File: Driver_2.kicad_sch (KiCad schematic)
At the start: 26 parts

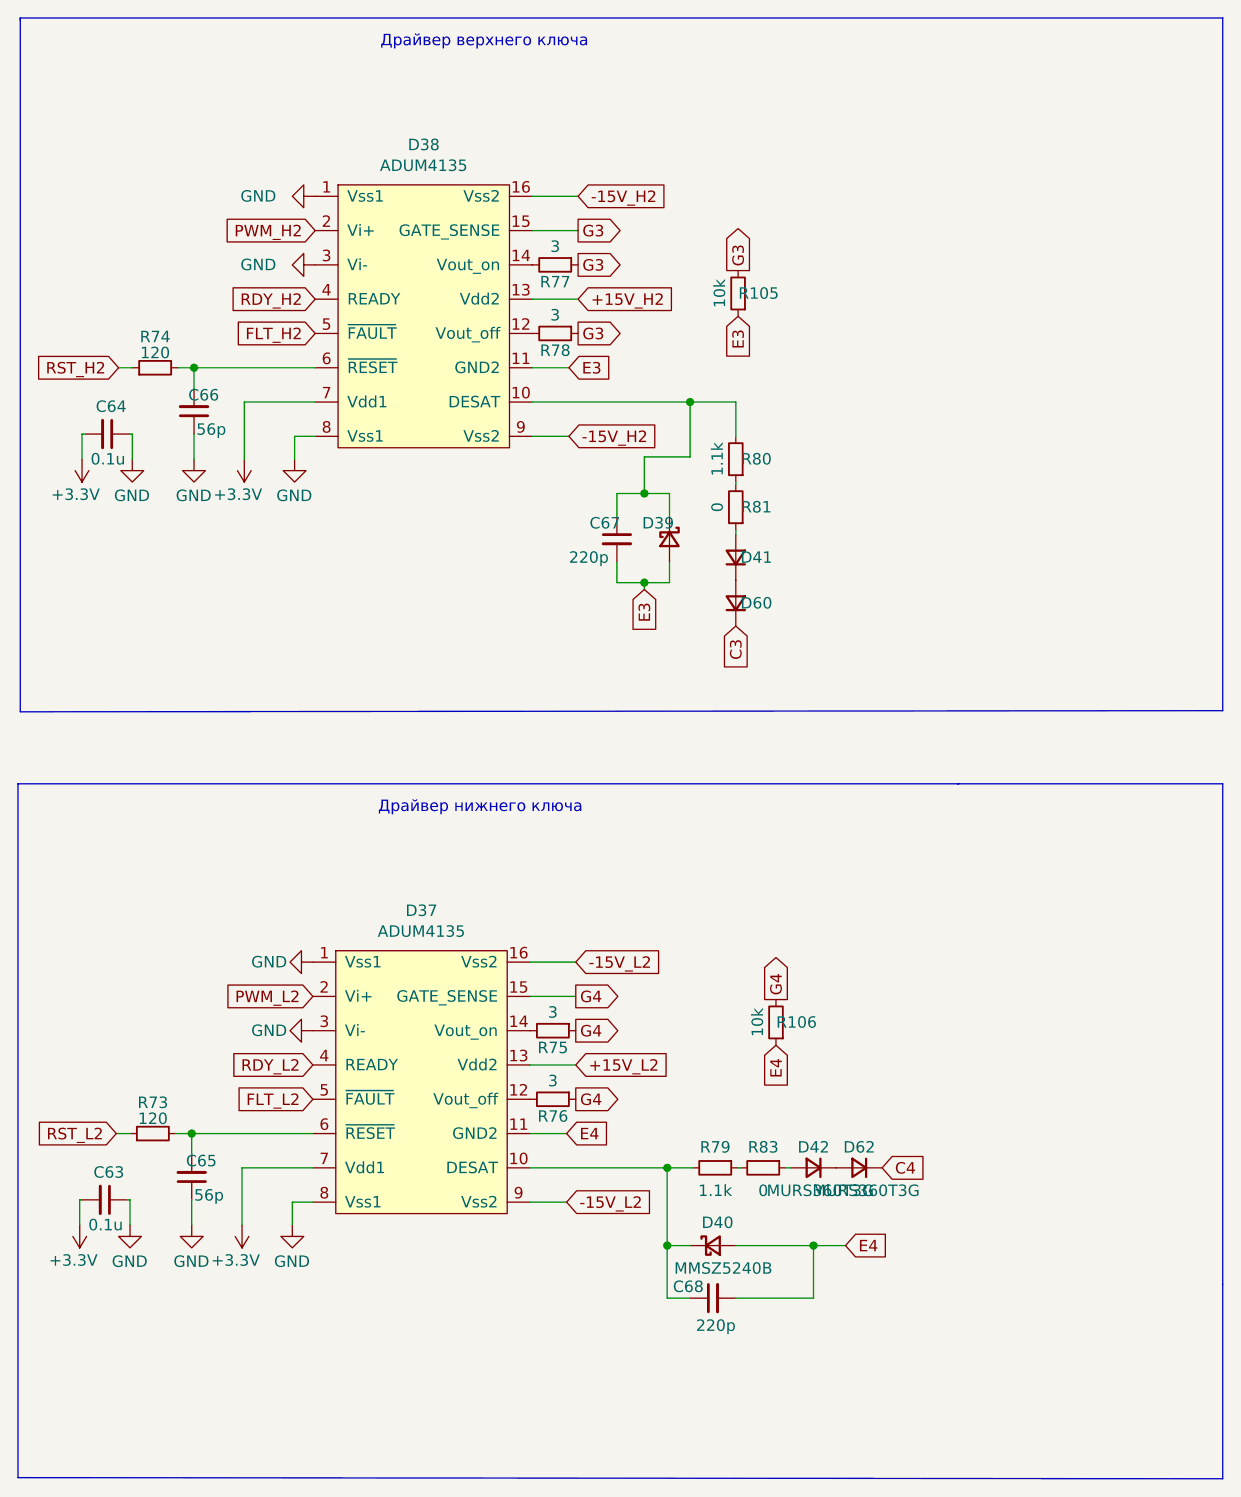
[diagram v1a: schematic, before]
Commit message: Поменял драйвера на китайские
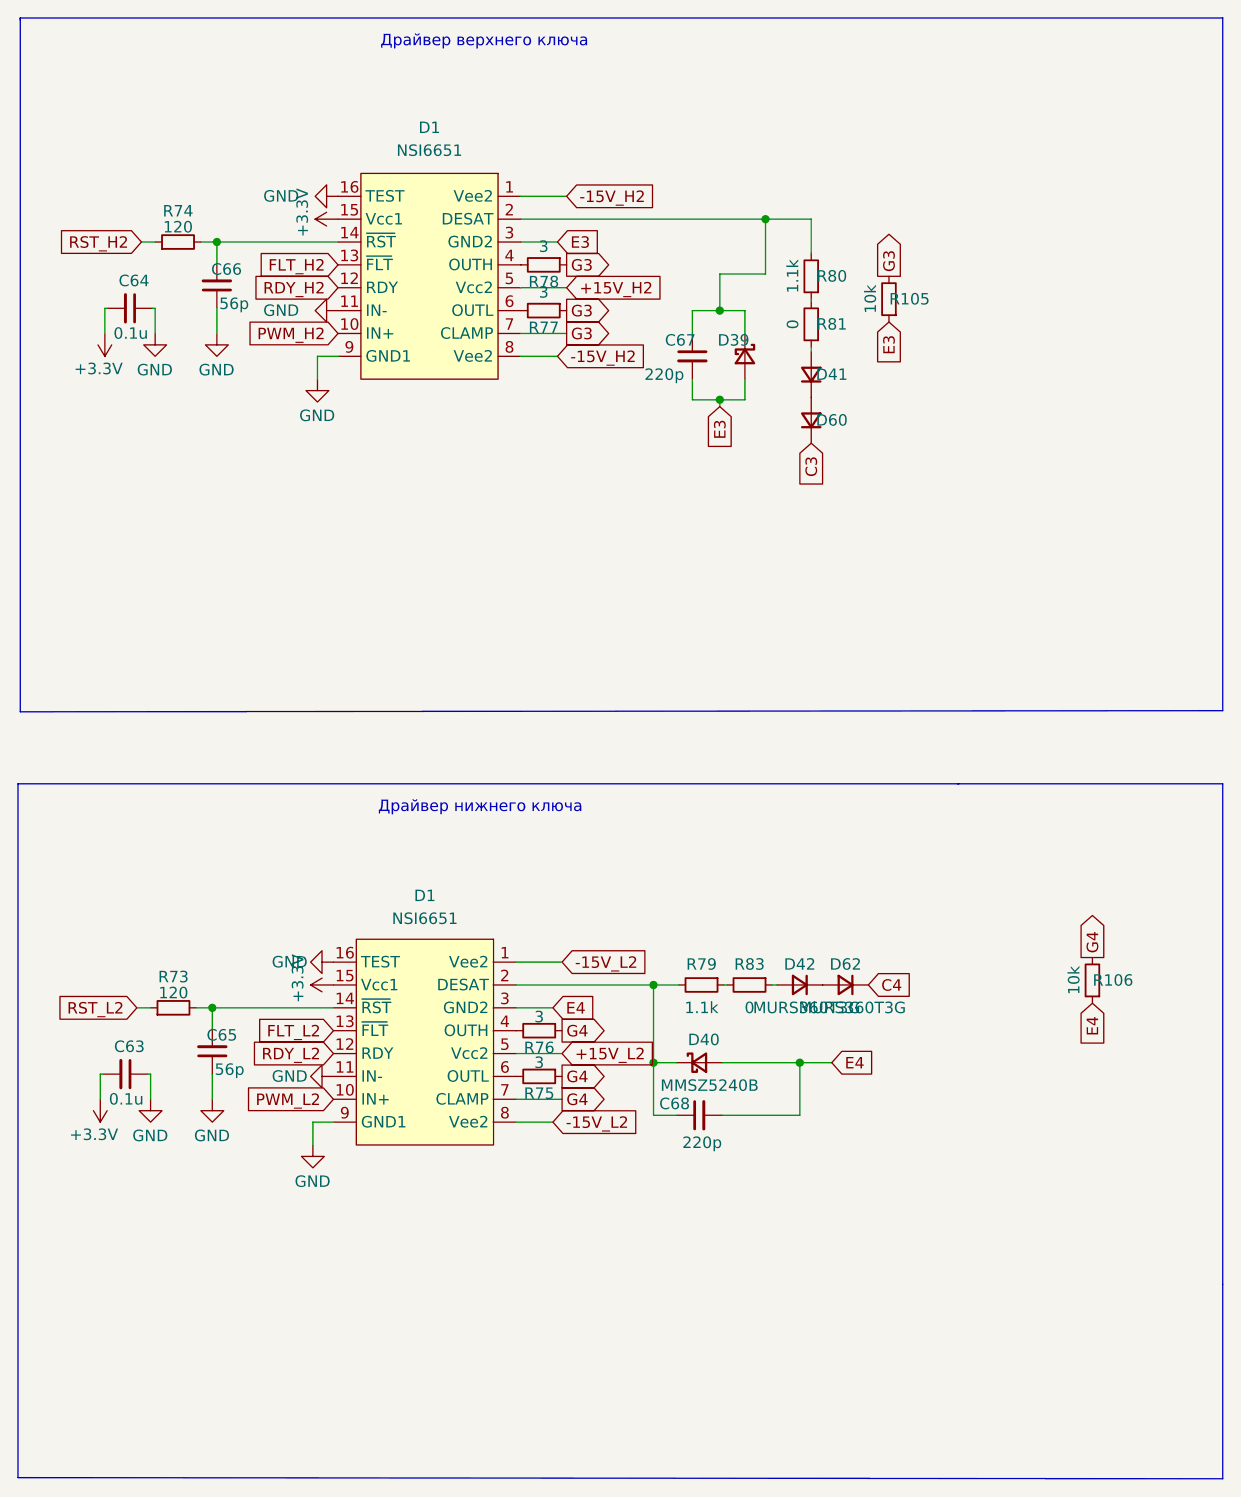
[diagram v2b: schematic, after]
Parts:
- removed D37, D38: ADUM4135, Package_SO:SOIC-16W_7.5x10.3mm_P1.27mm, symbol ADUM_Driver:ADUM4135
- added D1 (x2): NSI6651, Package_SO:SOIC-16W_7.5x10.3mm_P1.27mm, symbol Driver_My:NSI6651
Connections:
- net +15V_H2: now also D1.5 (Vcc2)
- net +15V_L2: now also D1.5 (Vcc2)
- net +3V3: now also D1.15 (Vcc1), D1.15 (Vcc1)
- net -15V_H2: now also D1.1 (Vee2), D1.8 (Vee2)
- net -15V_L2: now also D1.1 (Vee2), D1.8 (Vee2)
- net E3: now also D1.3 (GND2)
- net E4: now also D1.3 (GND2)
- net FLT_H2: now also D1.13 (~{FLT})
- net FLT_L2: now also D1.13 (~{FLT})
- net G3: now also D1.7 (CLAMP)
- net G4: now also D1.7 (CLAMP)
- net GND: now also D1.11 (IN-), D1.11 (IN-), D1.16 (TEST), D1.16 (TEST), D1.9 (GND1), D1.9 (GND1)
- net PWM_H2: now also D1.10 (IN+)
- net PWM_L2: now also D1.10 (IN+)
- net RDY_H2: now also D1.12 (RDY)
- net RDY_L2: now also D1.12 (RDY)
- net at R77.2: now also D1.6 (OUTL)
- net at C67.1, D39.1 (K), R80.2: now also D1.2 (DESAT)
- net at R78.2: now also D1.4 (OUTH)
- net at C66.2, R74.2: now also D1.14 (~{RST})
- net at R75.2: now also D1.6 (OUTL)
- net at C65.2, R73.2: now also D1.14 (~{RST})
- net at C68.1, D40.1 (K), R79.2: now also D1.2 (DESAT)
- net at R76.2: now also D1.4 (OUTH)
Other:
- moved on the sheet: C63, C64, C65, C66, C67, C68, D39, D40, D41, D42, D60, D62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

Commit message: Изменил схему
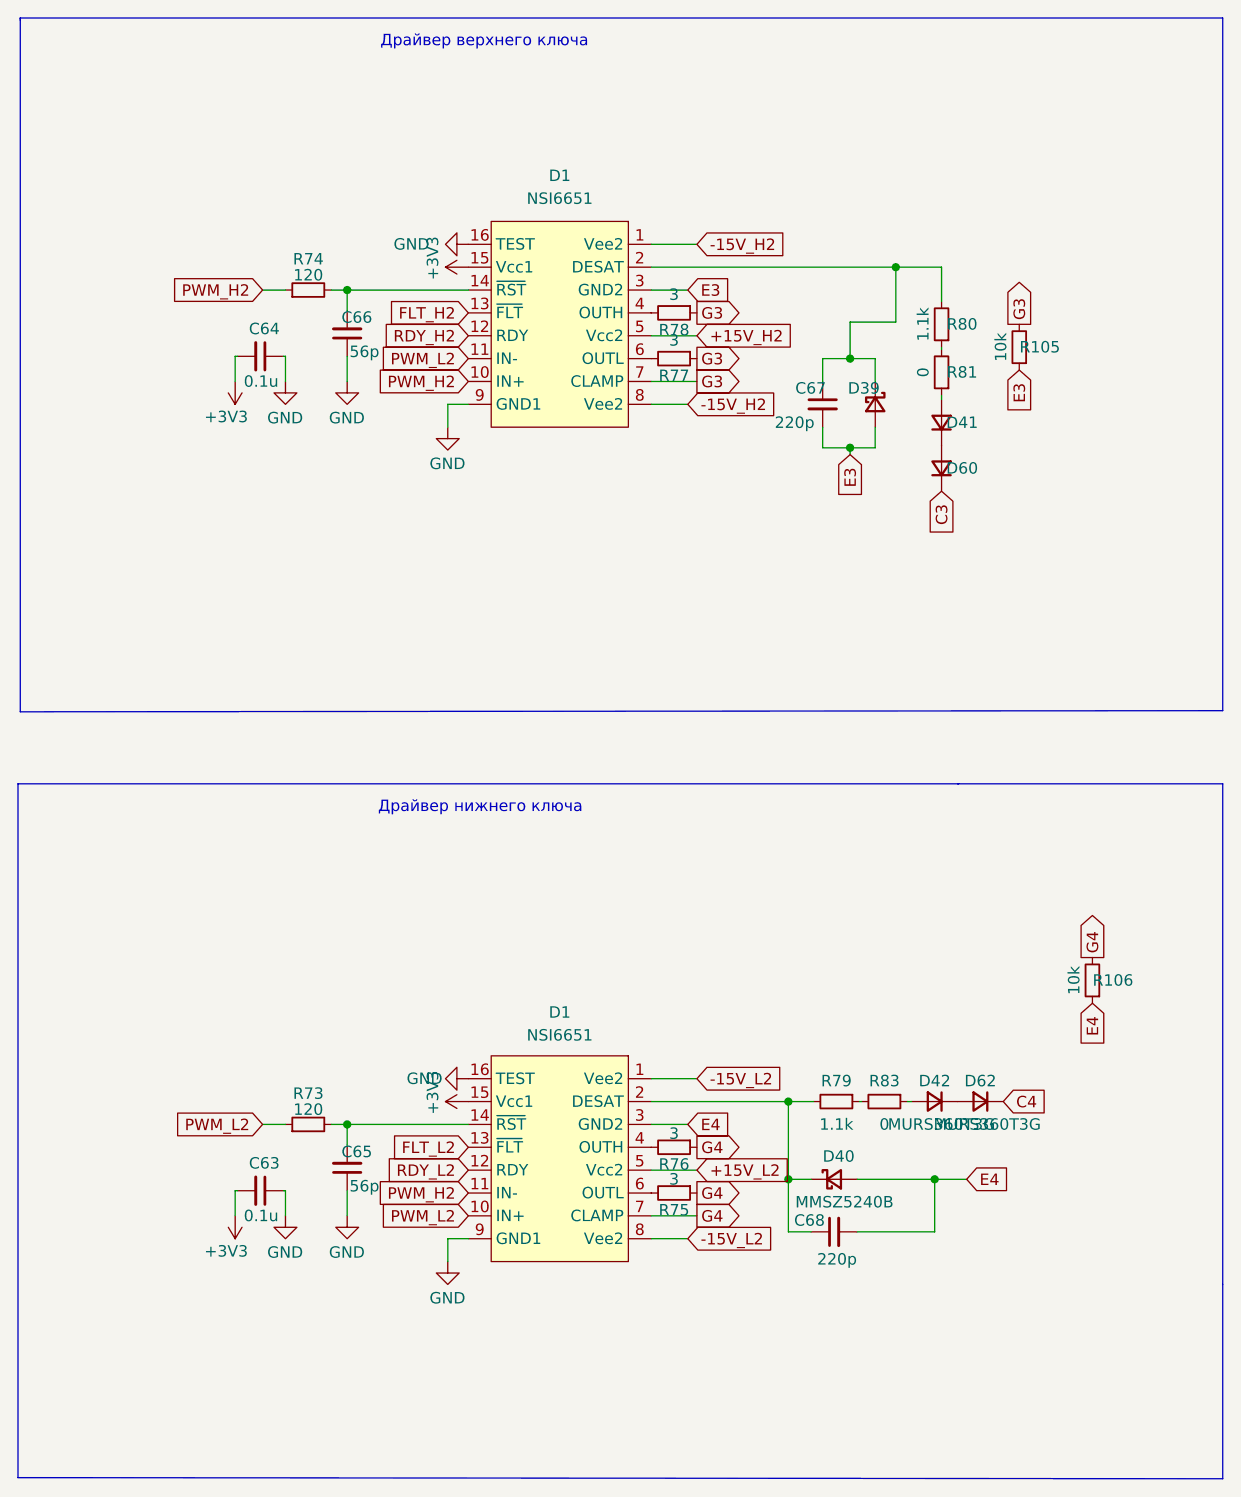
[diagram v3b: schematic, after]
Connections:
- net RST_H2 is gone; now on net PWM_H2: R74.1
- net RST_L2 is gone; now on net PWM_L2: R73.1
- net GND: no longer D1.11 (IN-), D1.11 (IN-)
- net PWM_H2: now also D1.11 (IN-)
- net PWM_L2: now also D1.11 (IN-)
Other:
- moved on the sheet: C63, C64, C65, C66, C67, C68, D1, D39, D40, D41, D42, D60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

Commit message: Разместил все три стойки в своей области
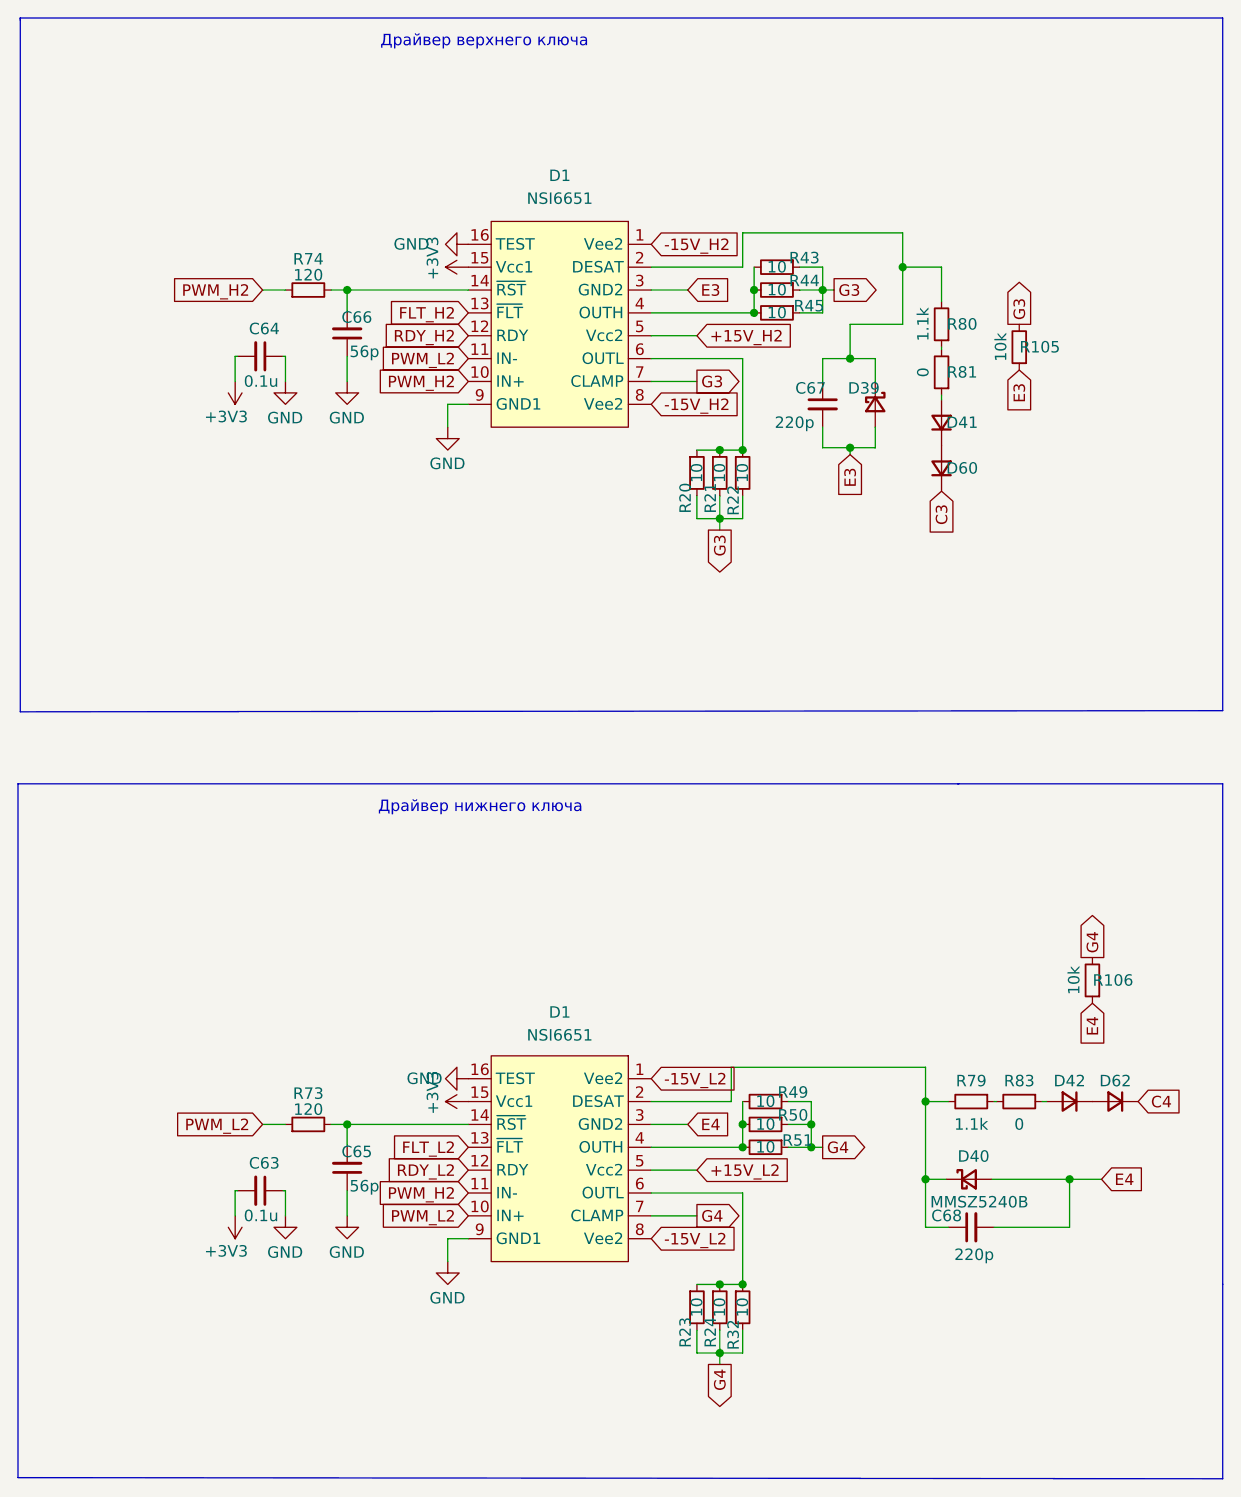
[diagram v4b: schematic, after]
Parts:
- removed R75, R76, R77, R78: 3, Resistor_SMD:R_2512_6332Metric_Pad1.40x3.35mm_HandSolder, symbol Device:R_Small
- added R20, R21, R22, R23, R24, R32, R43, R44, R45, R49, R50, R51: 10, Resistor_SMD:R_1206_3216Metric_Pad1.30x1.75mm_HandSolder, symbol Device:R_Small
- D41, D42, D60, D62: footprint Diode_SMD:D_SMC -> Diode_SMD:D_SMA_Handsoldering
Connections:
- net G3: now also R20.2, R21.2, R22.2, R43.1, R44.1, R45.1
- net G4: now also R23.2, R24.2, R32.2, R49.1, R50.1, R51.1
- net at D1.6 (OUTL): now also R20.1, R21.1, R22.1
- net at D1.6 (OUTL): now also R23.1, R24.1, R32.1
- net at D1.4 (OUTH): now also R43.2, R44.2, R45.2
- net at D1.4 (OUTH): now also R49.2, R50.2, R51.2
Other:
- moved on the sheet: C68, D40, D42, D62, R79, R83

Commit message: Убрал питание 3.3В
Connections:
- net +3V3 renamed +5V
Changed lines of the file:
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@@
 	)
 	(symbol
-		(lib_id "power:+3.3V")
+		(lib_id "power:+5V")
 		(at 55.372 156.21 180)
 		(unit 1)
@@
 		(on_board yes)
 		(dnp no)
-		(property "Reference" "#PWR0181"
+		(property "Reference" "#PWR181"
 			(at 55.372 152.4 0)
 			(effects
@@
 			)
 		)
-		(property "Value" "+3V3"
-			(at 51.943 160.147 0)
-			(effects
-				(font
-					(size 1.27 1.27)
-				)
-				(justify right)
+		(property "Value" "+5V"
+			(at 55.372 159.766 0)
+			(effects
+				(font
+					(size 1.27 1.27)
+				)
 			)
 		)
@@
 			)
 		)
-		(property "Description" ""
+		(property "Description" "Power symbol creates a global label with name \"+5V\""
 			(at 55.372 156.21 0)
 			(effects
@@
 			(project "Adapter"
 				(path "/e63e39d7-6ac0-4ffd-8aa3-1841a4541b55/7be86f5d-dd1f-4f1b-8cd0-4746349973df"
-					(reference "#PWR0181")
+					(reference "#PWR181")
 					(unit 1)
 				)
@@
 	)
 	(symbol
-		(lib_id "power:+3.3V")
+		(lib_id "power:+5V")
 		(at 81.28 50.8 90)
 		(unit 1)
@@
 		(on_board yes)
 		(dnp no)
-		(property "Reference" "#PWR0176"
+		(property "Reference" "#PWR176"
 			(at 85.09 50.8 0)
 			(effects
@@
 			)
 		)
-		(property "Value" "+3V3"
-			(at 77.343 47.371 0)
-			(effects
-				(font
-					(size 1.27 1.27)
-				)
-				(justify right)
+		(property "Value" "+5V"
+			(at 77.724 50.8 0)
+			(effects
+				(font
+					(size 1.27 1.27)
+				)
 			)
 		)
@@
 			)
 		)
-		(property "Description" ""
+		(property "Description" "Power symbol creates a global label with name \"+5V\""
 			(at 81.28 50.8 0)
 			(effects
@@
 			(project "Adapter"
 				(path "/e63e39d7-6ac0-4ffd-8aa3-1841a4541b55/7be86f5d-dd1f-4f1b-8cd0-4746349973df"
-					(reference "#PWR0176")
+					(reference "#PWR176")
 					(unit 1)
 				)
@@
 	)
 	(symbol
-		(lib_id "power:+3.3V")
+		(lib_id "power:+5V")
 		(at 55.372 63.5 180)
 		(unit 1)
@@
 		(on_board yes)
 		(dnp no)
-		(property "Reference" "#PWR0175"
+		(property "Reference" "#PWR175"
 			(at 55.372 59.69 0)
 			(effects
@@
 			)
 		)
-		(property "Value" "+3V3"
-			(at 51.943 67.437 0)
-			(effects
-				(font
-					(size 1.27 1.27)
-				)
-				(justify right)
+		(property "Value" "+5V"
+			(at 55.372 67.056 0)
+			(effects
+				(font
+					(size 1.27 1.27)
+				)
 			)
 		)
@@
 			)
 		)
-		(property "Description" ""
+		(property "Description" "Power symbol creates a global label with name \"+5V\""
 			(at 55.372 63.5 0)
 			(effects
@@
 			(project "Adapter"
 				(path "/e63e39d7-6ac0-4ffd-8aa3-1841a4541b55/7be86f5d-dd1f-4f1b-8cd0-4746349973df"
-					(reference "#PWR0175")
+					(reference "#PWR175")
 					(unit 1)
 				)
@@
 	)
 	(symbol
-		(lib_id "power:+3.3V")
+		(lib_id "power:+5V")
 		(at 81.28 143.51 90)
 		(unit 1)
@@
 		(on_board yes)
 		(dnp no)
-		(property "Reference" "#PWR0182"
+		(property "Reference" "#PWR182"
 			(at 85.09 143.51 0)
 			(effects
@@
 			)
 		)
-		(property "Value" "+3V3"
-			(at 77.343 140.081 0)
-			(effects
-				(font
-					(size 1.27 1.27)
-				)
-				(justify right)
+		(property "Value" "+5V"
+			(at 77.724 143.51 0)
+			(effects
+				(font
+					(size 1.27 1.27)
+				)
 			)
 		)
@@
 			)
 		)
-		(property "Description" ""
+		(property "Description" "Power symbol creates a global label with name \"+5V\""
 			(at 81.28 143.51 0)
 			(effects
@@
 			(project "Adapter"
 				(path "/e63e39d7-6ac0-4ffd-8aa3-1841a4541b55/7be86f5d-dd1f-4f1b-8cd0-4746349973df"
-					(reference "#PWR0182")
-					(unit 1)
-				)
+					(reference "#PWR182")
+					(unit 1)
+				)
